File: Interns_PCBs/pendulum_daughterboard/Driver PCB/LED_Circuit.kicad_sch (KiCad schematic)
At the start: 15 parts, among them IC1 AND GATES, IC2 NAND (Used as AND), IC3 NAND (Used as Inverter), IC4 OR, J4 Conn_01x04

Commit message: Friday Updates
24/06/22
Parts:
- J4: footprint TerminalBlock_TE-Connectivity:TerminalBlock_TE_282834-4_1x04_P2.54mm_Horizontal -> Connector_PinHeader_1.27mm:PinHeader_1x04_P1.27mm_Vertical
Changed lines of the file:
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@@
     (property "Reference" "J4" (id 0) (at 281.94 74.93 0))
     (property "Value" "Conn_01x04" (id 1) (at 281.94 77.47 0))
-    (property "Footprint" "TerminalBlock_TE-Connectivity:TerminalBlock_TE_282834-4_1x04_P2.54mm_Horizontal" (id 2) (at 281.94 86.36 0)
+    (property "Footprint" "Connector_PinHeader_1.27mm:PinHeader_1x04_P1.27mm_Vertical" (id 2) (at 281.94 86.36 0)
       (effects (font (size 1.27 1.27)) hide)
     )

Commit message: 01/07 UPDATES
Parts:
- J4: footprint Connector_PinHeader_1.27mm:PinHeader_1x04_P1.27mm_Vertical -> Connector_PinHeader_2.54mm:PinHeader_1x04_P2.54mm_Vertical
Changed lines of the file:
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@@
     (property "Reference" "J4" (id 0) (at 281.94 74.93 0))
     (property "Value" "Conn_01x04" (id 1) (at 281.94 77.47 0))
-    (property "Footprint" "Connector_PinHeader_1.27mm:PinHeader_1x04_P1.27mm_Vertical" (id 2) (at 281.94 86.36 0)
+    (property "Footprint" "Connector_PinHeader_2.54mm:PinHeader_1x04_P2.54mm_Vertical" (id 2) (at 281.94 86.36 0)
       (effects (font (size 1.27 1.27)) hide)
     )

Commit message: Changed Logic
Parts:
- removed C4, C5, C6, C7: 100nF, Capacitor_SMD:C_0805_2012Metric_Pad1.18x1.45mm_HandSolder, symbol Device:C
- removed IC1: AND GATES, ICPINS:SOIC127P600X175-14N, symbol CD74HC08QM96EP:CD74HC08QM96EP
- removed IC2: NAND (Used as AND), ICPINS:SOIC127P600X175-14N, symbol MC74ACT00DG:MC74ACT00DG
- removed IC3: NAND (Used as Inverter), ICPINS:SOIC127P600X175-14N, symbol MC74ACT00DG:MC74ACT00DG
- removed IC4: OR, ICPINS:SOIC127P600X175-14N, symbol MC74ACT00DG:MC74ACT00DG
- added U1: 4081, symbol 4xxx:4081
- added U2, U3: 4011, symbol 4xxx:4011
- added U4: 4071, symbol 4xxx:4011
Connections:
- net 5V: now also U1.14 (VDD), U2.14 (VDD), U3.14 (VDD), U4.14 (VDD)
- net GND: now also U1.7 (VSS), U2.7 (VSS), U3.7 (VSS), U4.7 (VSS)
- net STUDENT_ENABLE: now also U1.12, U1.5, U2.8, U3.1, U3.2, U3.5, U3.6, U3.8, U3.9
- net STU_LED_1: now also U1.6
- net STU_LED_2: now also U1.13
- net STU_LED_3: now also U2.9
- net SUP_LED_1: now also U1.1
- net SUP_LED_2: now also U1.8
- net SUP_LED_3: now also U2.1
- net OR_OUT_1: no longer names the net of D1.2 (A), J4.4 (Pin_4)
- net OR_OUT_1: now also U4.3
- net OR_OUT_2: no longer names the net of D2.2 (A), J4.3 (Pin_3)
- net OR_OUT_2: now also U4.4
- net OR_OUT_3: no longer names the net of D3.2 (A), J4.2 (Pin_2)
- net OR_OUT_3: now also U4.10
- new net: U1.2, U3.3
- new net: U1.3, U4.1
- new net: U2.4, U4.8
- new net: U2.3, U2.5, U2.6
- new net: U1.10, U4.5
- new net: U1.11, U4.6
- new net: U2.2, U3.10
- new net: U1.4, U4.2
- new net: U1.9, U3.4
- new net: U2.11, U4.9
- new net: U2.10, U2.12, U2.13
- no-connect marks 6 -> 0

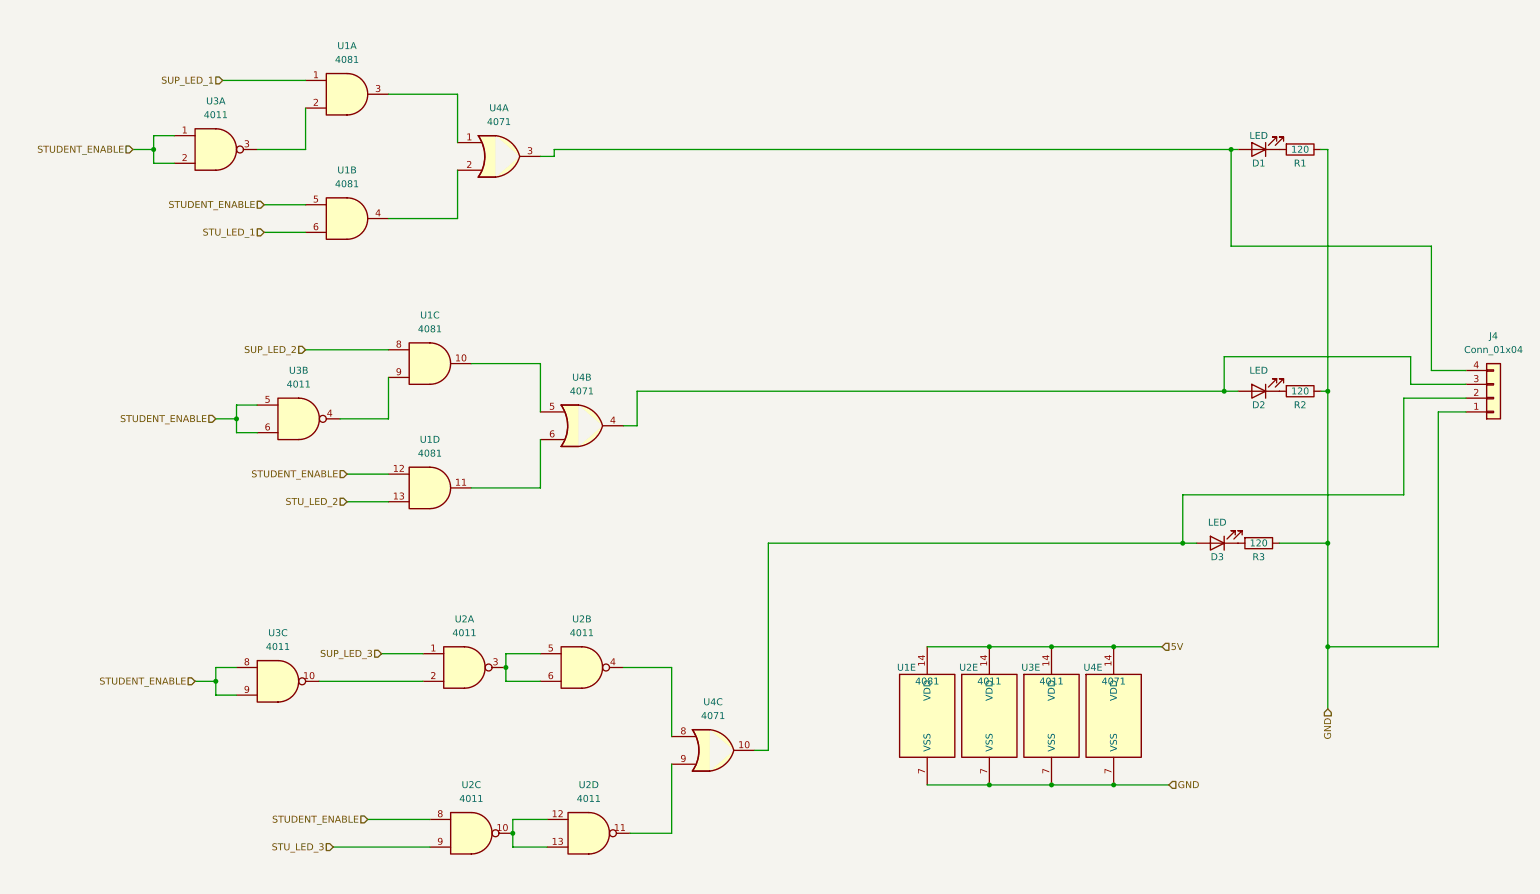
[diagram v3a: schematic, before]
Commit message: Pull down and Current Limiting Resistors
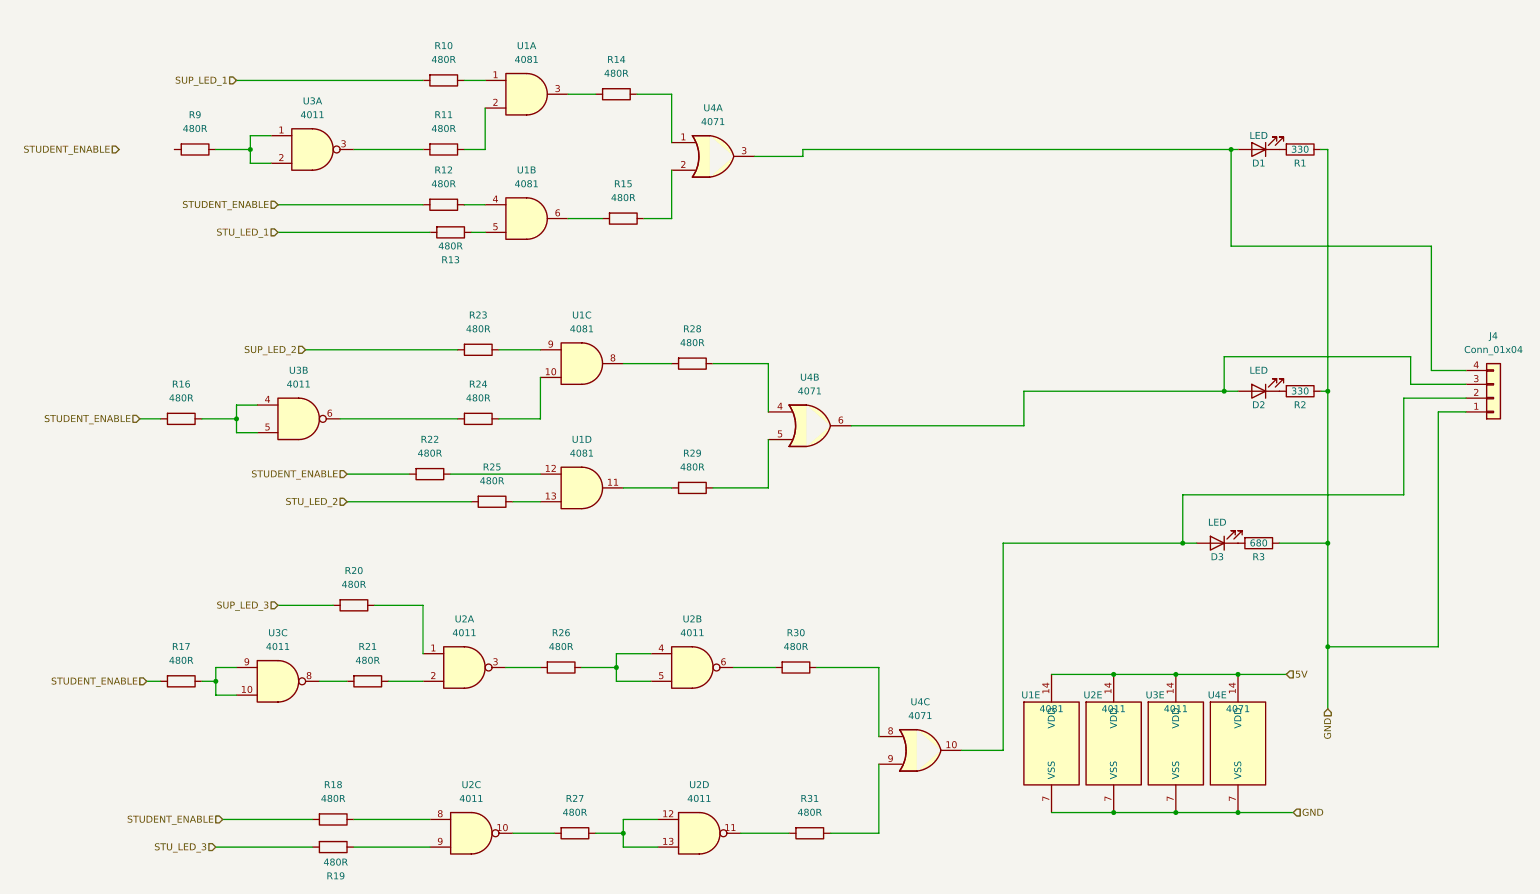
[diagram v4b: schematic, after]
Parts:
- added R10, R11, R12, R13, R14, R15, R16, R17, R18, R19, R20, R21, R22, R23, R24, R25, R26, R27, R28, R29, R30, R31, R9: 480R, symbol Device:R
- R1, R2: value 120 -> 330
- R3: value 120 -> 680
- U1, U2, U3, U4: footprint (none) -> Package_SO:SOIC127P600X175-14N
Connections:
- net STUDENT_ENABLE: now also R12.2, R16.2, R17.2, R18.2, R22.2; no longer U1.12, U1.5, U2.8, U3.1, U3.2, U3.5, U3.6, U3.8, U3.9
- net STU_LED_1: now also R13.2; no longer U1.6
- net STU_LED_2: now also R25.2; no longer U1.13
- net STU_LED_3: now also R19.2; no longer U2.9
- net SUP_LED_1: now also R10.2; no longer U1.1
- net SUP_LED_2: now also R23.2; no longer U1.8
- net SUP_LED_3: now also R20.2; no longer U2.1
- net at D2.2 (A), J4.3 (Pin_3): now also U4.6; no longer U4.4
- net at U1.2: now also R11.1; no longer U3.3
- net at U1.3: now also R14.2; no longer U4.1
- net at U2.4: now also U2.5, R26.1; no longer U4.8
- net at U4.5: now also R29.1; no longer U1.10
- net at U1.11: now also R29.2; no longer U4.6
- net at U3.10: now also U3.9, R17.1; no longer U2.2
- net at U1.4: now also R12.1; no longer U4.2
- net at U1.9: now also R23.1; no longer U3.4
- net at U4.9: now also R31.1; no longer U2.11
- net at U2.12, U2.13: now also R27.1; no longer U2.10
- new net: R13.1, U1.5
- new net: R22.1, U1.12
- new net: R10.1, U1.1
- new net: R27.2, U2.10
- new net: R30.2, U2.6
- new net: R20.1, U2.1
- new net: R18.1, U2.8
- new net: R31.2, U2.11
- new net: R28.1, U4.4
- new net: R21.2, U3.8
- new net: R15.2, U1.6
- new net: R28.2, U1.8
- new net: R15.1, U4.2
- new net: R30.1, U4.8
- new net: R9.1, U3.1, U3.2
- new net: R25.1, U1.13
- new net: R14.1, U4.1
- new net: R26.2, U2.3
- new net: R24.1, U1.10
- new net: R24.2, U3.6
- new net: R16.1, U3.4, U3.5
- new net: R21.1, U2.2
- new net: R19.1, U2.9
- new net: R11.2, U3.3
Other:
- moved on the sheet: U1A, U1B, U1C, U1D, U1E, U2B, U2D, U2E, U3A, U3E, U4A, U4B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
